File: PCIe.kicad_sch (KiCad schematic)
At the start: 12 parts, among them J25 Bus_M.2_Socket_M

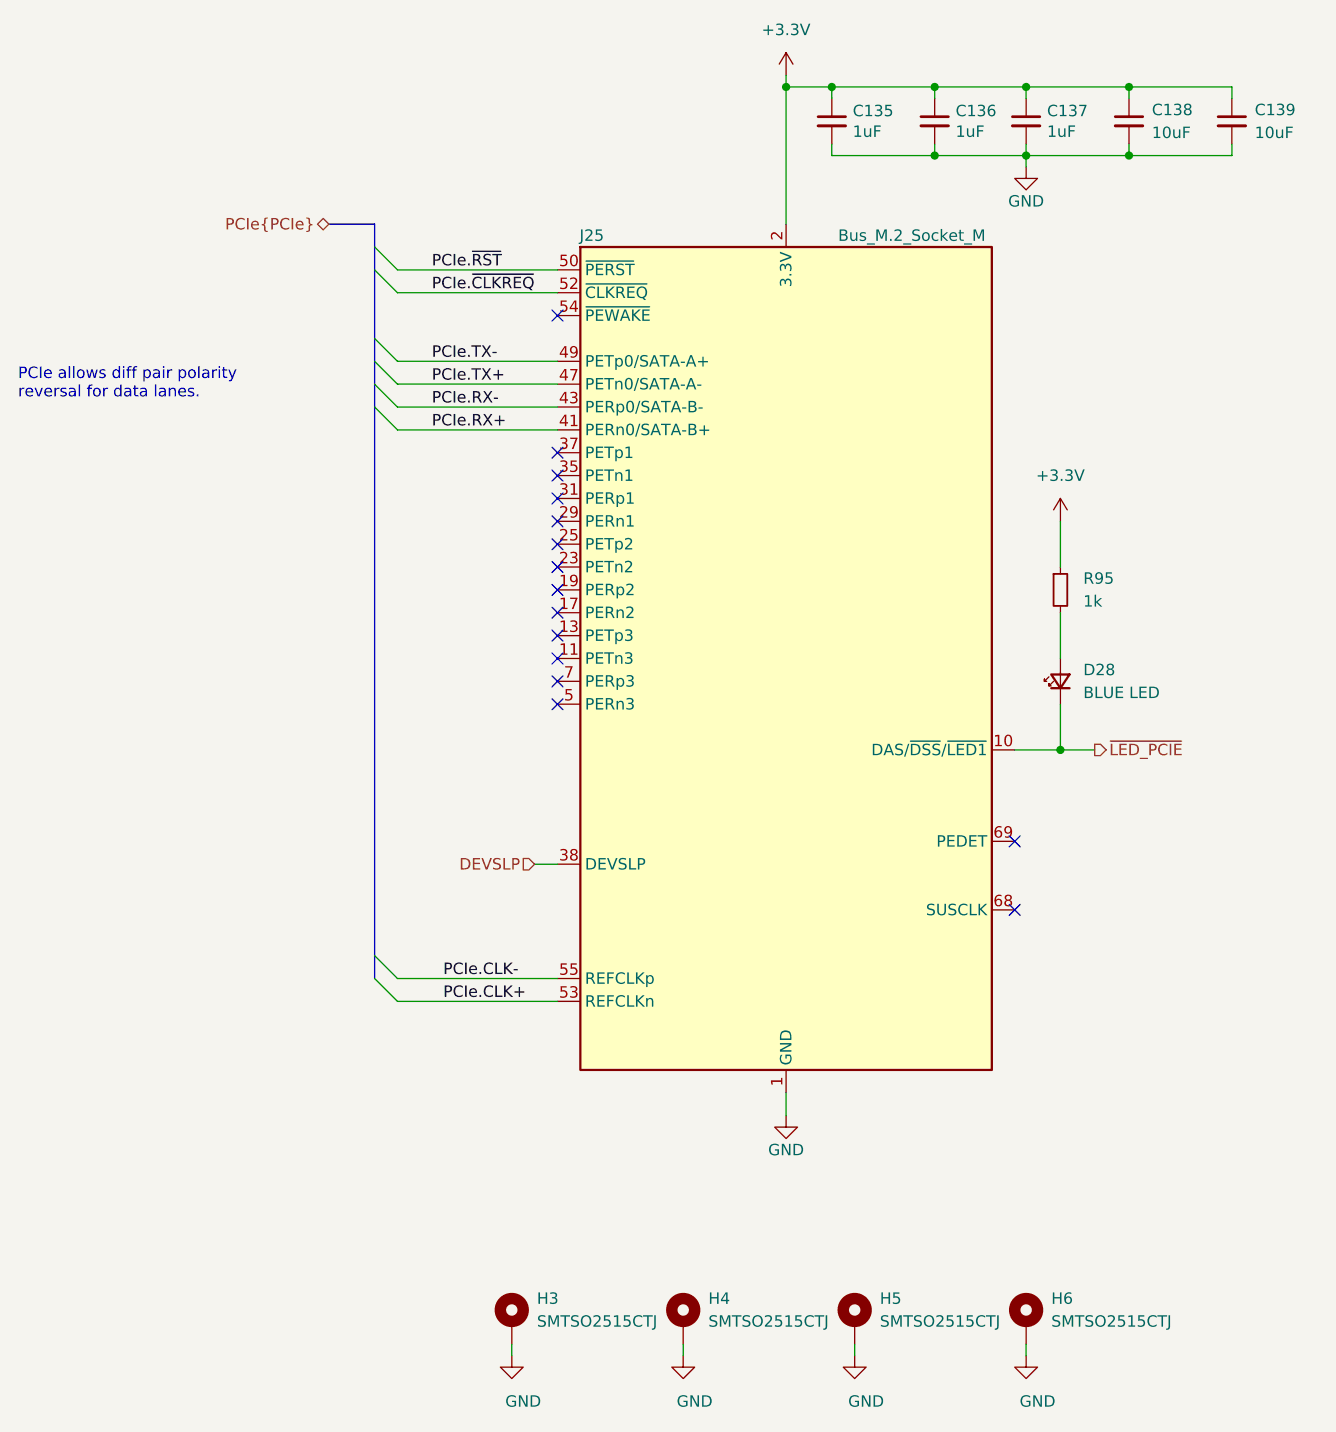
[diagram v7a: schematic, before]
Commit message: Final chores
- Reannotate components
- Improve USB2 connector skew matching
- Update sheet blocks
- Fix some diff-pair double-inversions
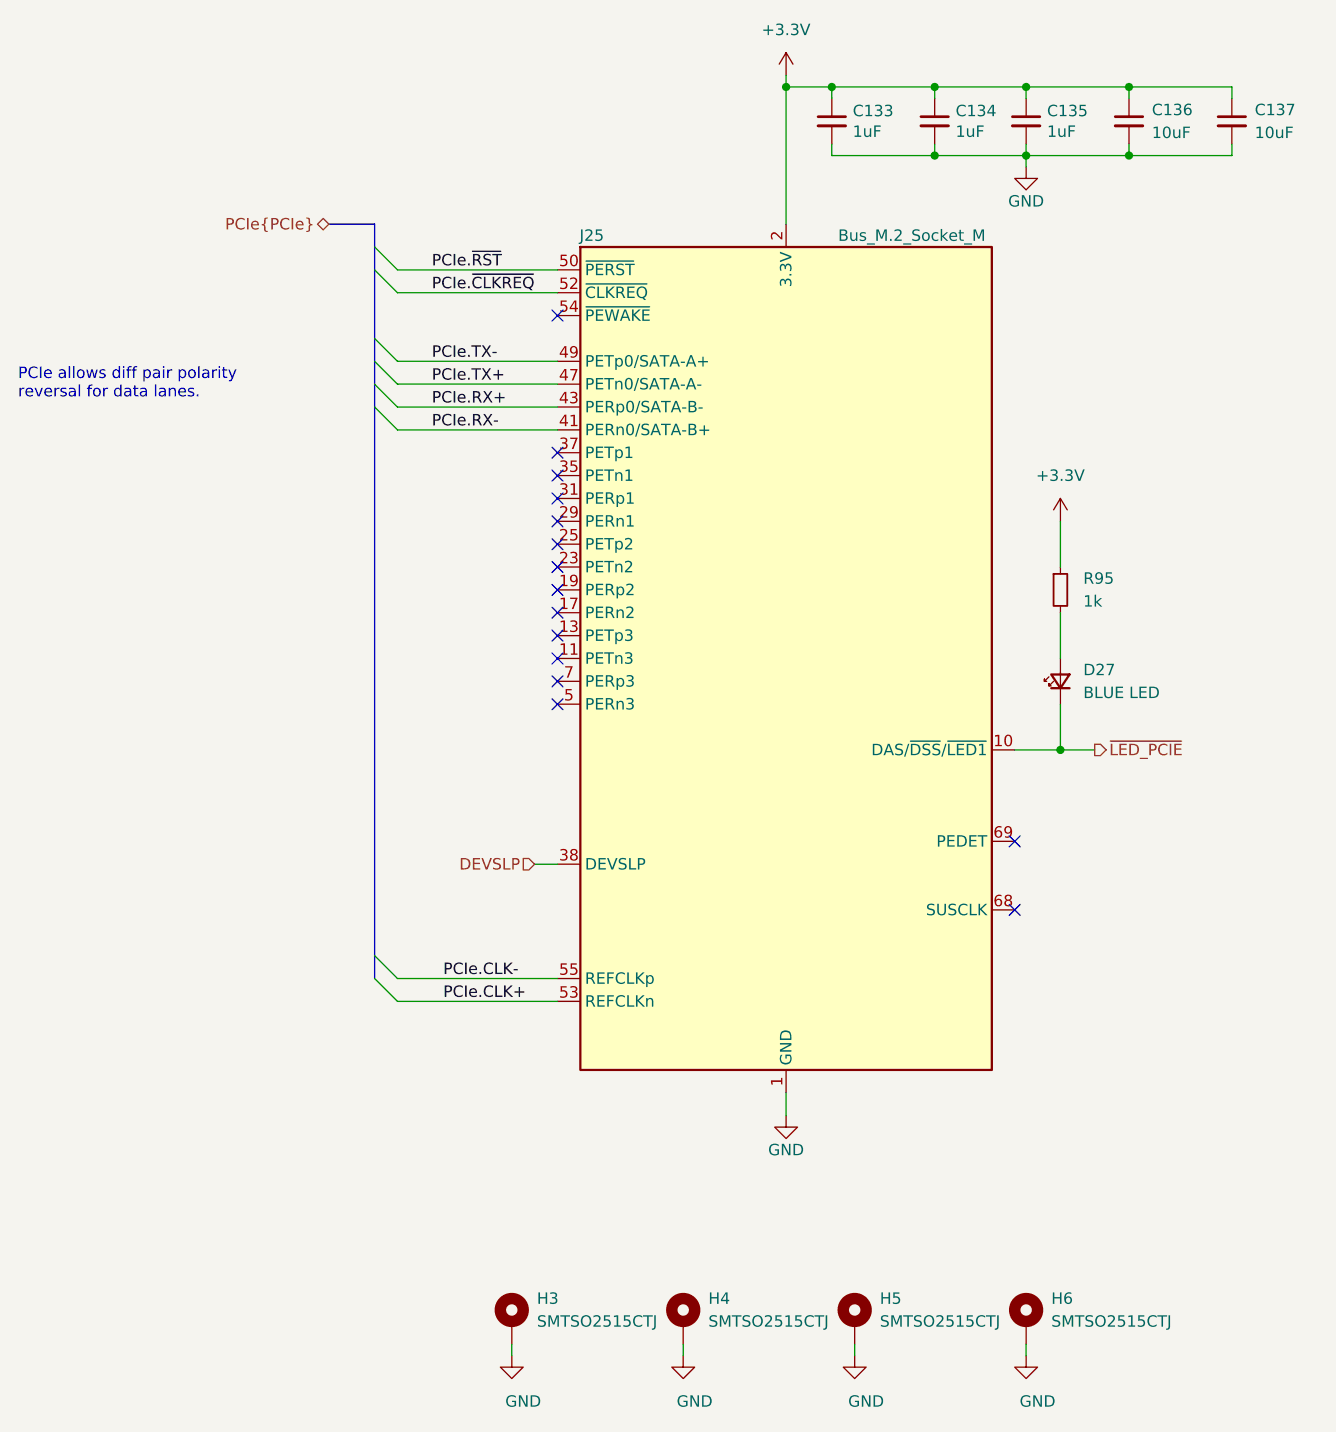
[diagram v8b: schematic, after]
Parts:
- renumbered C135 to C133, C136 to C134, C137 to C135, C138 to C136, C139 to C137, D28 to D27
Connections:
- net PCIe.RX+: now also J25.43 (PERp0/SATA-B-); no longer J25.41 (PERn0/SATA-B+)
- net PCIe.RX-: now also J25.41 (PERn0/SATA-B+); no longer J25.43 (PERp0/SATA-B-)
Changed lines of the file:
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@@
 	(title_block
 		(title "HALPI2")
-		(date "2025-03-27")
-		(rev "v0.2.0")
+		(date "2025-05-08")
+		(rev "v0.3.0")
 		(company "Hat Labs Oy")
 		(comment 1 "https://ohwr.org/cern_ohl_s_v2.pdf")
@@
 	)
 	(label "PCIe.RX-"
-		(at 74.93 63.5 0)
+		(at 74.93 66.04 0)
 		(effects
 			(font
@@
 	)
 	(label "PCIe.RX+"
-		(at 74.93 66.04 0)
+		(at 74.93 63.5 0)
 		(effects
 			(font
@@
 		(on_board yes)
 		(dnp no)
-		(property "Reference" "C135"
+		(property "Reference" "C133"
 			(at 121.7042 30.6006 0)
 			(effects
@@
 			(project "Yellow"
 				(path "/abc482bd-3f17-4d35-80db-1da3dcdb5c27/a1a835e0-c072-4609-9cb4-4b95bf746f54"
-					(reference "C135")
+					(reference "C133")
 					(unit 1)
 				)
@@
 		(on_board yes)
 		(dnp no)
-		(property "Reference" "C136"
+		(property "Reference" "C134"
 			(at 133.1342 30.6006 0)
 			(effects
@@
 			(project "Yellow"
 				(path "/abc482bd-3f17-4d35-80db-1da3dcdb5c27/a1a835e0-c072-4609-9cb4-4b95bf746f54"
-					(reference "C136")
+					(reference "C134")
 					(unit 1)
 				)
@@
 		(on_board yes)
 		(dnp no)
-		(property "Reference" "D28"
+		(property "Reference" "D27"
 			(at 147.32 92.71 90)
 			(effects
@@
 			(project "Yellow"
 				(path "/abc482bd-3f17-4d35-80db-1da3dcdb5c27/a1a835e0-c072-4609-9cb4-4b95bf746f54"
-					(reference "D28")
+					(reference "D27")
 					(unit 1)
 				)
@@
 		(dnp no)
 		(fields_autoplaced yes)
-		(property "Reference" "C139"
+		(property "Reference" "C137"
 			(at 166.37 30.4862 0)
 			(effects
@@
 			(project "HALPI2"
 				(path "/abc482bd-3f17-4d35-80db-1da3dcdb5c27/a1a835e0-c072-4609-9cb4-4b95bf746f54"
-					(reference "C139")
+					(reference "C137")
 					(unit 1)
 				)
@@
 		(on_board yes)
 		(dnp no)
-		(property "Reference" "#PWR0242"
+		(property "Reference" "#PWR0236"
 			(at 102.87 175.26 0)
 			(effects
@@
 			(project "HALPI2"
 				(path "/abc482bd-3f17-4d35-80db-1da3dcdb5c27/a1a835e0-c072-4609-9cb4-4b95bf746f54"
-					(reference "#PWR0242")
+					(reference "#PWR0236")
 					(unit 1)
 				)
@@
 		(on_board yes)
 		(dnp no)
-		(property "Reference" "C137"
+		(property "Reference" "C135"
 			(at 143.2942 30.6006 0)
 			(effects
@@
 			(project "Yellow"
 				(path "/abc482bd-3f17-4d35-80db-1da3dcdb5c27/a1a835e0-c072-4609-9cb4-4b95bf746f54"
-					(reference "C137")
+					(reference "C135")
 					(unit 1)
 				)
@@
 		(dnp no)
 		(fields_autoplaced yes)
-		(property "Reference" "#PWR0248"
+		(property "Reference" "#PWR0242"
 			(at 144.78 80.01 0)
 			(effects
@@
 			(project "HALPI2"
 				(path "/abc482bd-3f17-4d35-80db-1da3dcdb5c27/a1a835e0-c072-4609-9cb4-4b95bf746f54"
-					(reference "#PWR0248")
+					(reference "#PWR0242")
 					(unit 1)
 				)
@@
 		(dnp no)
 		(fields_autoplaced yes)
-		(property "Reference" "#PWR0243"
+		(property "Reference" "#PWR0237"
 			(at 114.3 30.48 0)
 			(effects
@@
 			(project ""
 				(path "/abc482bd-3f17-4d35-80db-1da3dcdb5c27/a1a835e0-c072-4609-9cb4-4b95bf746f54"
-					(reference "#PWR0243")
+					(reference "#PWR0237")
 					(unit 1)
 				)
@@
 		(on_board yes)
 		(dnp no)
-		(property "Reference" "#PWR0246"
+		(property "Reference" "#PWR0240"
 			(at 140.97 43.18 0)
 			(effects
@@
 			(project "Yellow"
 				(path "/abc482bd-3f17-4d35-80db-1da3dcdb5c27/a1a835e0-c072-4609-9cb4-4b95bf746f54"
-					(reference "#PWR0246")
+					(reference "#PWR0240")
 					(unit 1)
 				)
@@
 		(on_board yes)
 		(dnp no)
-		(property "Reference" "#PWR0247"
+		(property "Reference" "#PWR0241"
 			(at 140.97 175.26 0)
 			(effects
@@
 			(project "HALPI2"
 				(path "/abc482bd-3f17-4d35-80db-1da3dcdb5c27/a1a835e0-c072-4609-9cb4-4b95bf746f54"
-					(reference "#PWR0247")
+					(reference "#PWR0241")
 					(unit 1)
 				)
@@
 		(on_board yes)
 		(dnp no)
-		(property "Reference" "#PWR0245"
+		(property "Reference" "#PWR0239"
 			(at 121.92 175.26 0)
 			(effects
@@
 			(project "HALPI2"
 				(path "/abc482bd-3f17-4d35-80db-1da3dcdb5c27/a1a835e0-c072-4609-9cb4-4b95bf746f54"
-					(reference "#PWR0245")
+					(reference "#PWR0239")
 					(unit 1)
 				)
@@
 		(on_board yes)
 		(dnp no)
-		(property "Reference" "#PWR0241"
+		(property "Reference" "#PWR0235"
 			(at 83.82 175.26 0)
 			(effects
@@
 			(project "HALPI2"
 				(path "/abc482bd-3f17-4d35-80db-1da3dcdb5c27/a1a835e0-c072-4609-9cb4-4b95bf746f54"
-					(reference "#PWR0241")
+					(reference "#PWR0235")
 					(unit 1)
 				)
@@
 		(dnp no)
 		(fields_autoplaced yes)
-		(property "Reference" "C138"
+		(property "Reference" "C136"
 			(at 154.94 30.4862 0)
 			(effects
@@
 			(project "HALPI2"
 				(path "/abc482bd-3f17-4d35-80db-1da3dcdb5c27/a1a835e0-c072-4609-9cb4-4b95bf746f54"
-					(reference "C138")
+					(reference "C136")
 					(unit 1)
 				)
@@
 		(on_board yes)
 		(dnp no)
-		(property "Reference" "#PWR0244"
+		(property "Reference" "#PWR0238"
 			(at 114.3 148.59 0)
 			(effects
@@
 			(project "Yellow"
 				(path "/abc482bd-3f17-4d35-80db-1da3dcdb5c27/a1a835e0-c072-4609-9cb4-4b95bf746f54"
-					(reference "#PWR0244")
+					(reference "#PWR0238")
 					(unit 1)
 				)
